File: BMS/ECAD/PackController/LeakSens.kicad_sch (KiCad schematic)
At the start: 6 parts

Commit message: close to finish BMS master, only some footprints needed
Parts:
- renumbered C5 to C1601, R12 to R1601, R10 to R1602, R11 to R1603, R13 to R1604, R30 to R1605
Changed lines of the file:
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@@
 		(in_pos_files no)
 		(dnp no)
-		(property "Reference" "R12"
+		(property "Reference" "R1601"
 			(at 143.51 81.28 90)
 			(hide yes)
@@
 			(project "Pack_Controller"
 				(path "/58a1c93e-baba-4d23-9191-955e00968735/84895c30-1551-4ee7-9bdb-3f8b53d8ebdd/4f74f959-10cb-474a-9e4a-07aad2d2b472"
-					(reference "R12")
-					(unit 1)
-				)
-				(path "/58a1c93e-baba-4d23-9191-955e00968735/84895c30-1551-4ee7-9bdb-3f8b53d8ebdd/f4edf52c-f084-49c8-89dd-48baa523d797"
-					(reference "R15")
+					(reference "R1601")
+					(unit 1)
+				)
+				(path "/58a1c93e-baba-4d23-9191-955e00968735/84895c30-1551-4ee7-9bdb-3f8b53d8ebdd/f4edf52c-f084-49c8-89dd-48baa523d797"
+					(reference "R1701")
 					(unit 1)
 				)
@@
 		(in_pos_files yes)
 		(dnp no)
-		(property "Reference" "#PWR05"
+		(property "Reference" "#PWR01601"
 			(at 214.63 102.87 0)
 			(hide yes)
@@
 			(project "Pack_Controller"
 				(path "/58a1c93e-baba-4d23-9191-955e00968735/84895c30-1551-4ee7-9bdb-3f8b53d8ebdd/4f74f959-10cb-474a-9e4a-07aad2d2b472"
-					(reference "#PWR05")
-					(unit 1)
-				)
-				(path "/58a1c93e-baba-4d23-9191-955e00968735/84895c30-1551-4ee7-9bdb-3f8b53d8ebdd/f4edf52c-f084-49c8-89dd-48baa523d797"
-					(reference "#PWR07")
+					(reference "#PWR01601")
+					(unit 1)
+				)
+				(path "/58a1c93e-baba-4d23-9191-955e00968735/84895c30-1551-4ee7-9bdb-3f8b53d8ebdd/f4edf52c-f084-49c8-89dd-48baa523d797"
+					(reference "#PWR01701")
 					(unit 1)
 				)
@@
 		(in_pos_files no)
 		(dnp no)
-		(property "Reference" "R13"
+		(property "Reference" "R1604"
 			(at 143.51 86.36 90)
 			(hide yes)
@@
 			(project "Pack_Controller"
 				(path "/58a1c93e-baba-4d23-9191-955e00968735/84895c30-1551-4ee7-9bdb-3f8b53d8ebdd/4f74f959-10cb-474a-9e4a-07aad2d2b472"
-					(reference "R13")
-					(unit 1)
-				)
-				(path "/58a1c93e-baba-4d23-9191-955e00968735/84895c30-1551-4ee7-9bdb-3f8b53d8ebdd/f4edf52c-f084-49c8-89dd-48baa523d797"
-					(reference "R16")
+					(reference "R1604")
+					(unit 1)
+				)
+				(path "/58a1c93e-baba-4d23-9191-955e00968735/84895c30-1551-4ee7-9bdb-3f8b53d8ebdd/f4edf52c-f084-49c8-89dd-48baa523d797"
+					(reference "R1704")
 					(unit 1)
 				)
@@
 		(in_pos_files yes)
 		(dnp no)
-		(property "Reference" "C5"
+		(property "Reference" "C1601"
 			(at 199.39 93.98 90)
 			(show_name no)
@@
 			(project "Pack_Controller"
 				(path "/58a1c93e-baba-4d23-9191-955e00968735/84895c30-1551-4ee7-9bdb-3f8b53d8ebdd/4f74f959-10cb-474a-9e4a-07aad2d2b472"
-					(reference "C5")
-					(unit 1)
-				)
-				(path "/58a1c93e-baba-4d23-9191-955e00968735/84895c30-1551-4ee7-9bdb-3f8b53d8ebdd/f4edf52c-f084-49c8-89dd-48baa523d797"
-					(reference "C18")
+					(reference "C1601")
+					(unit 1)
+				)
+				(path "/58a1c93e-baba-4d23-9191-955e00968735/84895c30-1551-4ee7-9bdb-3f8b53d8ebdd/f4edf52c-f084-49c8-89dd-48baa523d797"
+					(reference "C1701")
 					(unit 1)
 				)
@@
 		(in_pos_files yes)
 		(dnp no)
-		(property "Reference" "R30"
+		(property "Reference" "R1605"
 			(at 190.5 88.9 90)
 			(show_name no)
@@
 			(project "Pack_Controller"
 				(path "/58a1c93e-baba-4d23-9191-955e00968735/84895c30-1551-4ee7-9bdb-3f8b53d8ebdd/4f74f959-10cb-474a-9e4a-07aad2d2b472"
-					(reference "R30")
-					(unit 1)
-				)
-				(path "/58a1c93e-baba-4d23-9191-955e00968735/84895c30-1551-4ee7-9bdb-3f8b53d8ebdd/f4edf52c-f084-49c8-89dd-48baa523d797"
-					(reference "R31")
+					(reference "R1605")
+					(unit 1)
+				)
+				(path "/58a1c93e-baba-4d23-9191-955e00968735/84895c30-1551-4ee7-9bdb-3f8b53d8ebdd/f4edf52c-f084-49c8-89dd-48baa523d797"
+					(reference "R1705")
 					(unit 1)
 				)
@@
 		(in_pos_files yes)
 		(dnp no)
-		(property "Reference" "R11"
+		(property "Reference" "R1603"
 			(at 203.2 83.82 90)
 			(show_name no)
@@
 			(project "Pack_Controller"
 				(path "/58a1c93e-baba-4d23-9191-955e00968735/84895c30-1551-4ee7-9bdb-3f8b53d8ebdd/4f74f959-10cb-474a-9e4a-07aad2d2b472"
-					(reference "R11")
-					(unit 1)
-				)
-				(path "/58a1c93e-baba-4d23-9191-955e00968735/84895c30-1551-4ee7-9bdb-3f8b53d8ebdd/f4edf52c-f084-49c8-89dd-48baa523d797"
-					(reference "R17")
+					(reference "R1603")
+					(unit 1)
+				)
+				(path "/58a1c93e-baba-4d23-9191-955e00968735/84895c30-1551-4ee7-9bdb-3f8b53d8ebdd/f4edf52c-f084-49c8-89dd-48baa523d797"
+					(reference "R1703")
 					(unit 1)
 				)
@@
 		(in_pos_files yes)
 		(dnp no)
-		(property "Reference" "R10"
+		(property "Reference" "R1602"
 			(at 95.25 83.82 90)
 			(show_name no)
@@
 			(project "Pack_Controller"
 				(path "/58a1c93e-baba-4d23-9191-955e00968735/84895c30-1551-4ee7-9bdb-3f8b53d8ebdd/4f74f959-10cb-474a-9e4a-07aad2d2b472"
-					(reference "R10")
-					(unit 1)
-				)
-				(path "/58a1c93e-baba-4d23-9191-955e00968735/84895c30-1551-4ee7-9bdb-3f8b53d8ebdd/f4edf52c-f084-49c8-89dd-48baa523d797"
-					(reference "R14")
-					(unit 1)
-				)
+					(reference "R1602")
+					(unit 1)
+				)
+				(path "/58a1c93e-baba-4d23-9191-955e00968735/84895c30-1551-4ee7-9bdb-3f8b53d8ebdd/f4edf52c-f084-49c8-89dd-48baa523d797"
+					(reference "R1702")
+					(unit 1)
+				)

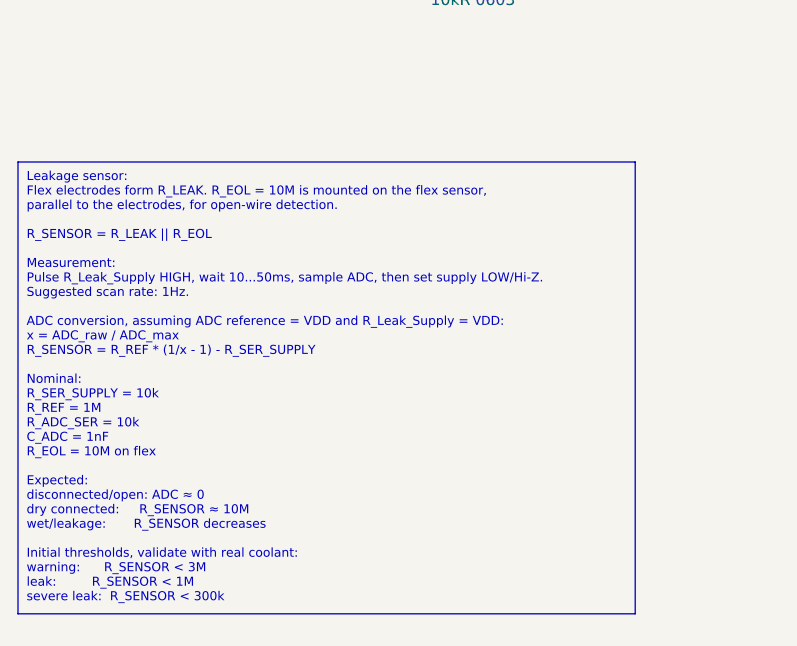
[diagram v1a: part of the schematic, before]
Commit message: finalised schematic of pack controller
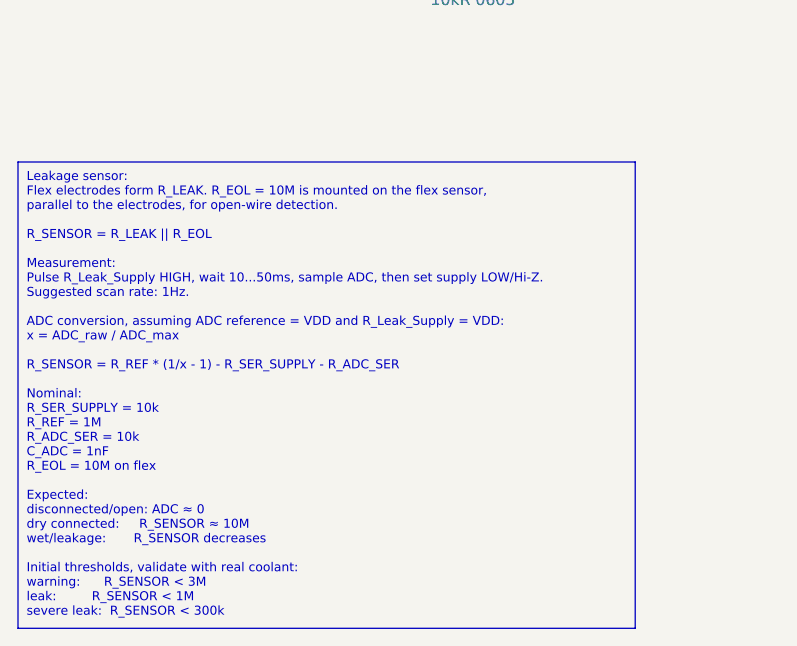
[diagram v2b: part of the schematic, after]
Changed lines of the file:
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@@
 		)
 	)
-	(text_box "Leakage sensor:\nFlex electrodes form R_LEAK. R_EOL = 10M is mounted on the flex sensor,\nparallel to the electrodes, for open-wire detection.\n\nR_SENSOR = R_LEAK || R_EOL\n\nMeasurement:\nPulse R_Leak_Supply HIGH, wait 10...50ms, sample ADC, then set supply LOW/Hi-Z.\nSuggested scan rate: 1Hz.\n\nADC conversion, assuming ADC reference = VDD and R_Leak_Supply = VDD:\nx = ADC_raw / ADC_max\nR_SENSOR = R_REF * (1/x - 1) - R_SER_SUPPLY\n\nNominal:\nR_SER_SUPPLY = 10k\nR_REF = 1M\nR_ADC_SER = 10k\nC_ADC = 1nF\nR_EOL = 10M on flex\n\nExpected:\ndisconnected/open: ADC ≈ 0\ndry connected:     R_SENSOR ≈ 10M\nwet/leakage:       R_SENSOR decreases\n\nInitial thresholds, validate with real coolant:\nwarning:      R_SENSOR < 3M\nleak:         R_SENSOR < 1M\nsevere leak:  R_SENSOR < 300k"
+	(text_box "Leakage sensor:\nFlex electrodes form R_LEAK. R_EOL = 10M is mounted on the flex sensor,\nparallel to the electrodes, for open-wire detection.\n\nR_SENSOR = R_LEAK || R_EOL\n\nMeasurement:\nPulse R_Leak_Supply HIGH, wait 10...50ms, sample ADC, then set supply LOW/Hi-Z.\nSuggested scan rate: 1Hz.\n\nADC conversion, assuming ADC reference = VDD and R_Leak_Supply = VDD:\nx = ADC_raw / ADC_max\n\nR_SENSOR = R_REF * (1/x - 1) - R_SER_SUPPLY - R_ADC_SER\n\nNominal:\nR_SER_SUPPLY = 10k\nR_REF = 1M\nR_ADC_SER = 10k\nC_ADC = 1nF\nR_EOL = 10M on flex\n\nExpected:\ndisconnected/open: ADC ≈ 0\ndry connected:     R_SENSOR ≈ 10M\nwet/leakage:       R_SENSOR decreases\n\nInitial thresholds, validate with real coolant:\nwarning:      R_SENSOR < 3M\nleak:         R_SENSOR < 1M\nsevere leak:  R_SENSOR < 300k"
 		(exclude_from_sim no)
 		(at 44.45 104.14 0)
-		(size 68.58 50.2022)
+		(size 68.58 51.8121)
 		(margins 0.9525 0.9525 0.9525 0.9525)
 		(stroke

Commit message: add rule areas for hv separation
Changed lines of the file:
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@@
 		)
 	)
-	(text_box "Leakage sensor:\nFlex electrodes form R_LEAK. R_EOL = 10M is mounted on the flex sensor,\nparallel to the electrodes, for open-wire detection.\n\nR_SENSOR = R_LEAK || R_EOL\n\nMeasurement:\nPulse R_Leak_Supply HIGH, wait 10...50ms, sample ADC, then set supply LOW/Hi-Z.\nSuggested scan rate: 1Hz.\n\nADC conversion, assuming ADC reference = VDD and R_Leak_Supply = VDD:\nx = ADC_raw / ADC_max\n\nR_SENSOR = R_REF * (1/x - 1) - R_SER_SUPPLY - R_ADC_SER\n\nNominal:\nR_SER_SUPPLY = 10k\nR_REF = 1M\nR_ADC_SER = 10k\nC_ADC = 1nF\nR_EOL = 10M on flex\n\nExpected:\ndisconnected/open: ADC ≈ 0\ndry connected:     R_SENSOR ≈ 10M\nwet/leakage:       R_SENSOR decreases\n\nInitial thresholds, validate with real coolant:\nwarning:      R_SENSOR < 3M\nleak:         R_SENSOR < 1M\nsevere leak:  R_SENSOR < 300k"
+	(text_box "Leakage sensor:\nFlex electrodes form R_LEAK. R_EOL = 10M is mounted on the flex sensor,\nparallel to the electrodes, for open-wire detection.\n\nR_SENSOR = R_LEAK || R_EOL\n\nMeasurement:\nPulse R_Leak_Supply HIGH, wait 10...50ms, sample ADC, then set supply LOW/Hi-Z.\nSuggested scan rate: 1Hz.\n\nADC conversion, assuming ADC reference = VDD and R_Leak_Supply = VDD:\nx = ADC_CODE / ADC_MAX\n\nR_SENSOR = R_REF × (1/x - 1)- R_SER_SUPPLY\n\nNominal:\nR_SER_SUPPLY = 10k\nR_REF = 1M\nR_ADC_SER = 10k\nC_ADC = 1nF\nR_EOL = 10M on flex\n\nExpected:\ndisconnected/open: ADC ≈ 0\ndry connected:     R_SENSOR ≈ 10M\nwet/leakage:       R_SENSOR decreases\n\nInitial thresholds, validate with real coolant:\nwarning:      R_SENSOR < 3M\nleak:         R_SENSOR < 1M\nsevere leak:  R_SENSOR < 300k"
 		(exclude_from_sim no)
 		(at 44.45 104.14 0)
